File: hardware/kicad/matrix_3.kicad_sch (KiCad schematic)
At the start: 139 parts, among them U7 IS31FL3741A

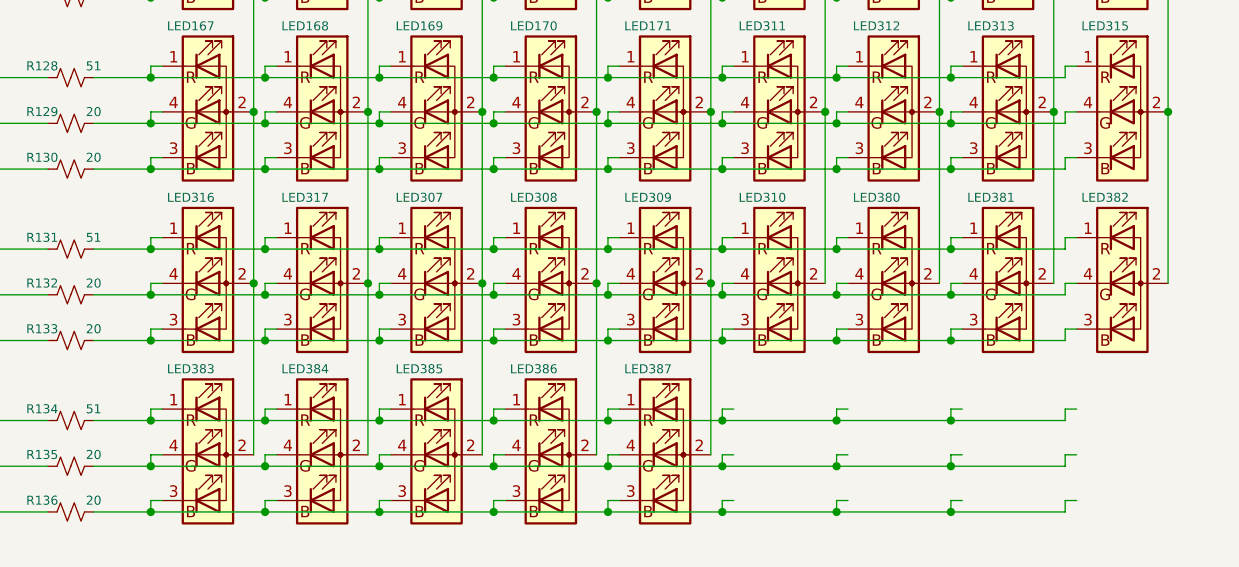
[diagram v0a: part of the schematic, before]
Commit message: update new led numbers
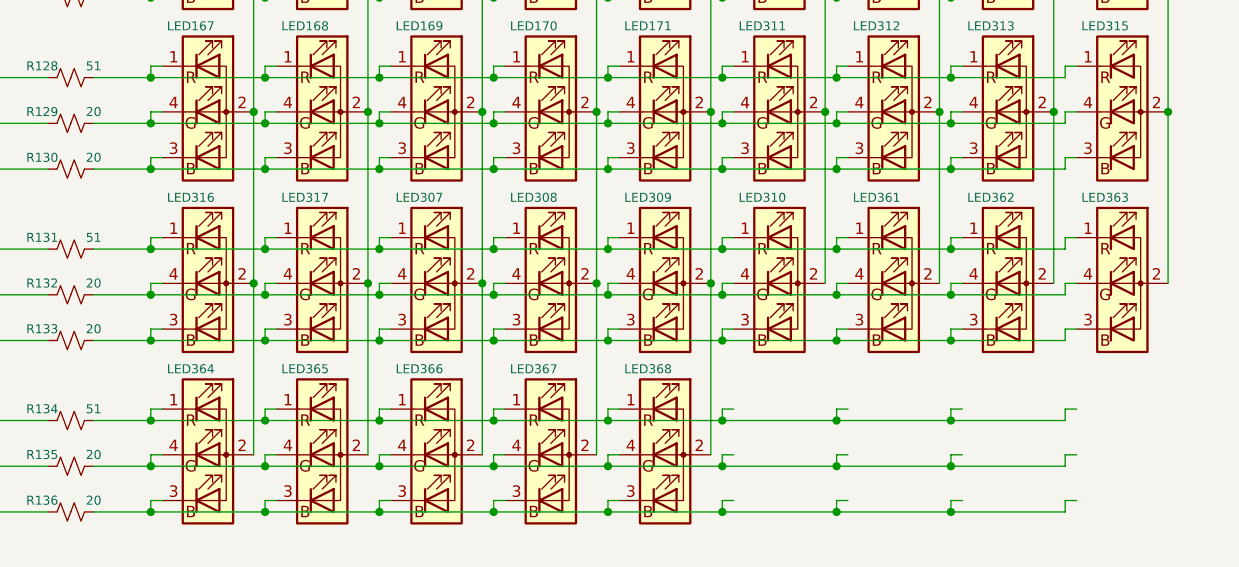
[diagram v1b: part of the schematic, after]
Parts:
- renumbered LED380 to LED361, LED381 to LED362, LED382 to LED363, LED383 to LED364, LED384 to LED365, LED385 to LED366, LED386 to LED367, LED387 to LED368
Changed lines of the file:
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@@
 		(on_board yes)
 		(dnp no)
-		(property "Reference" "LED380"
+		(property "Reference" "LED361"
 			(at 226.695 197.485 0)
 			(effects
@@
 			(project "traffic_paradise"
 				(path "/911505fc-874d-4338-908e-12054bdd5112/8dd6618c-1a80-4fae-a98a-23e19309c792"
-					(reference "LED380")
+					(reference "LED361")
 					(unit 1)
 				)
@@
 		(on_board yes)
 		(dnp no)
-		(property "Reference" "LED384"
+		(property "Reference" "LED365"
 			(at 163.195 216.535 0)
 			(effects
@@
 			(project "traffic_paradise"
 				(path "/911505fc-874d-4338-908e-12054bdd5112/8dd6618c-1a80-4fae-a98a-23e19309c792"
-					(reference "LED384")
+					(reference "LED365")
 					(unit 1)
 				)
@@
 		(on_board yes)
 		(dnp no)
-		(property "Reference" "LED383"
+		(property "Reference" "LED364"
 			(at 150.495 216.535 0)
 			(effects
@@
 			(project "traffic_paradise"
 				(path "/911505fc-874d-4338-908e-12054bdd5112/8dd6618c-1a80-4fae-a98a-23e19309c792"
-					(reference "LED383")
+					(reference "LED364")
 					(unit 1)
 				)
@@
 		(on_board yes)
 		(dnp no)
-		(property "Reference" "LED387"
+		(property "Reference" "LED368"
 			(at 201.295 216.535 0)
 			(effects
@@
 			(project "traffic_paradise"
 				(path "/911505fc-874d-4338-908e-12054bdd5112/8dd6618c-1a80-4fae-a98a-23e19309c792"
-					(reference "LED387")
+					(reference "LED368")
 					(unit 1)
 				)
@@
 		(on_board yes)
 		(dnp no)
-		(property "Reference" "LED381"
+		(property "Reference" "LED362"
 			(at 239.395 197.485 0)
 			(effects
@@
 			(project "traffic_paradise"
 				(path "/911505fc-874d-4338-908e-12054bdd5112/8dd6618c-1a80-4fae-a98a-23e19309c792"
-					(reference "LED381")
+					(reference "LED362")
 					(unit 1)
 				)
@@
 		(on_board yes)
 		(dnp no)
-		(property "Reference" "LED382"
+		(property "Reference" "LED363"
 			(at 252.095 197.485 0)
 			(effects
@@
 			(project "traffic_paradise"
 				(path "/911505fc-874d-4338-908e-12054bdd5112/8dd6618c-1a80-4fae-a98a-23e19309c792"
-					(reference "LED382")
+					(reference "LED363")
 					(unit 1)
 				)
@@
 		(on_board yes)
 		(dnp no)
-		(property "Reference" "LED386"
+		(property "Reference" "LED367"
 			(at 188.595 216.535 0)
 			(effects
@@
 			(project "traffic_paradise"
 				(path "/911505fc-874d-4338-908e-12054bdd5112/8dd6618c-1a80-4fae-a98a-23e19309c792"
-					(reference "LED386")
+					(reference "LED367")
 					(unit 1)
 				)
@@
 		(on_board yes)
 		(dnp no)
-		(property "Reference" "LED385"
+		(property "Reference" "LED366"
 			(at 175.895 216.535 0)
 			(effects
@@
 			(project "traffic_paradise"
 				(path "/911505fc-874d-4338-908e-12054bdd5112/8dd6618c-1a80-4fae-a98a-23e19309c792"
-					(reference "LED385")
+					(reference "LED366")
 					(unit 1)
 				)
